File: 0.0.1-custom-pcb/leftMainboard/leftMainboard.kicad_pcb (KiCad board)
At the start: 2 copper layers, 45 x 75.3 mm, 84 parts, among them J1 USB-C USB2 receptacle (footpr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, J10 HC-FPC-0.5-12P-FH20, J2 53398-0371, J3 GPIO / SWD 2x6 1.27mm, J7 HC-FPC-0.5-14P-FH20, J8 HC-FPC-0.5-12P-FH20, J9 HC-FPC-0.5-12P-FH20, Q1 BSS138 (guess), Q2 P-channel MOSFET (guess), Q3 P-channel MOSFET (guess), SW1 TK-6580A-1, SW2 Reset tactile 4x4mm (estimate), U1 SY7088DGC, U2 TP4056-42-ESOP8, U3 PRTR5V0U2X, U4 MDBT50Q-P1MV2, U5 74CBTLV1G125GV (probable b25 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, Y1 32.768kHz (guess)

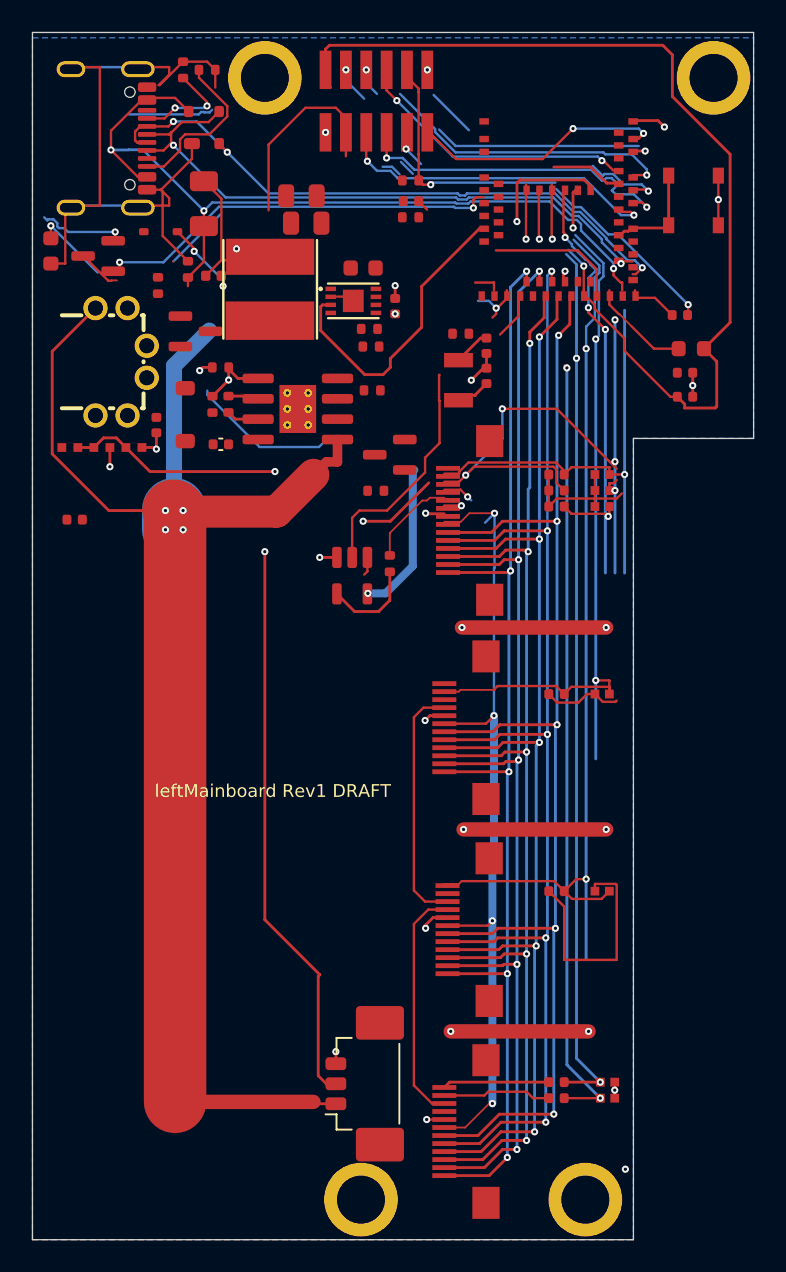
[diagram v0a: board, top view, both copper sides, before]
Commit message: update more components to be correct
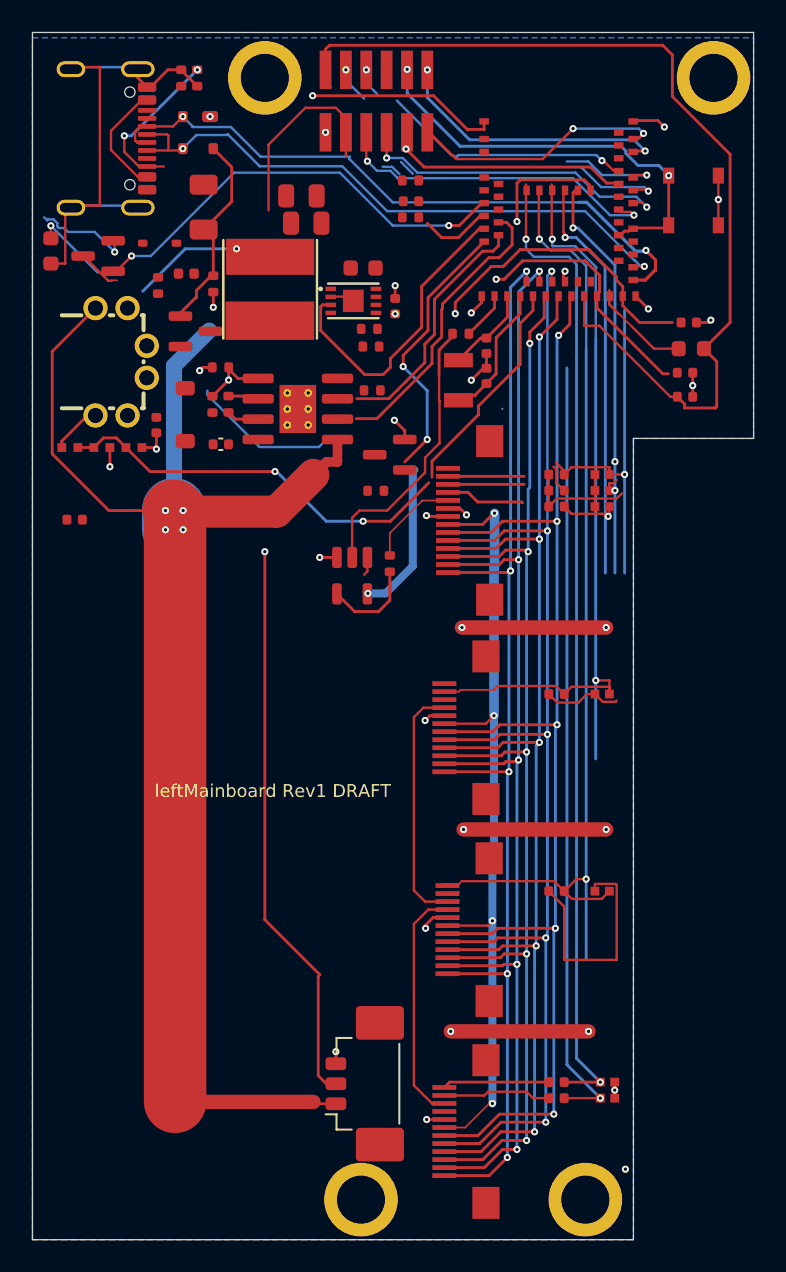
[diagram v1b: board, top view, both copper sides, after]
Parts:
- moved R11 1.82 mm to (61.1, 65.5), turned to -90 degrees
- moved L2 1.71 mm to (59.5, 64.8)
- moved R4 0.80 mm to (60.1, 52.6), turned to -90 degrees
- moved C10 0.72 mm to (90.8, 67.9), turned to 180 degrees
- moved D3 0.72 mm to (57.8, 63.0)
- moved R3 0.52 mm to (59.1, 52.6)
- moved U3 0.48 mm to (60.2, 56.0), turned to -90 degrees
- moved F1 0.22 mm to (60.5, 60.7)
- turned R22 to 180 degrees
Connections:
- ? pad 1: GND -> unconnected-(U4-P0.04-Pad20) (x3)
- ? pad 1: GND -> VBAT
- C8 pad 2: XL1 -> XL2
- C9 pad 2: XL2 -> XL1
- R8 pad 1: VDDH -> LED_DATA_MCU
- R8 pad 2: VDDH_FILTERED -> LED_DATA_MCU
- Y1 pad 1: XL1 -> XL2
- Y1 pad 2: XL2 -> XL1
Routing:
- net unconnected-(U4-P0.04-Pad20): track 0.00 -> 39.2 mm, vias 0 -> 1
- net GND: track 119.0 -> 100.0 mm, vias 19 -> 25
- net unconnected-(U4-P0.02-Pad11): track 0.00 -> 18.1 mm
- net unconnected-(U4-P0.30-Pad14): track 0.00 -> 17.0 mm, vias 0 -> 2
- net SWDIO: track 0.85 -> 17.6 mm
- net VBUS_USB: track 54.7 -> 39.0 mm, vias 3 -> 1
- net unconnected-(U4-P0.28-Pad13): track 0.00 -> 15.4 mm
- net unconnected-(U4-P0.09-Pad52): track 12.9 -> 0.00 mm
- net EXT3: track 20.6 -> 8.12 mm
- net VDDH_FILTERED: track 11.9 -> 0.00 mm, vias 1 -> 0
- net VDDH: track 25.6 -> 35.9 mm, vias 2 -> 3
- net EXT6: track 5.85 -> 15.5 mm
- net C1: track 42.6 -> 33.4 mm, vias 6 -> 3
- net VBUS_FUSED: track 9.00 -> 0.00 mm
- net VEXT_2V4: track 85.8 -> 77.3 mm, vias 3 -> 2
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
